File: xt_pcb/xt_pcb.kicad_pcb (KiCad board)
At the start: 2 copper layers, 197 parts, among them J1 Conn_01x04_Socket, SW1 SW_Push, SW10 SW_Push, SW11 SW_Push, SW12 SW_Push, SW13 SW_Push, SW14 SW_Push, SW15 SW_Push, SW16 SW_Push, SW17 SW_Push, SW19 SW_Push, SW2 SW_Push, SW20 SW_Push, SW21 SW_Push, SW22 SW_Push, SW23 SW_Push, SW24 SW_Push, SW25 SW_Push, SW26 SW_Push, SW27 SW_Push, SW28 SW_Push, SW29 SW_Push, SW3 SW_Push, SW30 SW_Push, SW31 SW_Push, SW32 SW_Push, SW33 SW_Push, SW34 SW_Push, SW35 SW_Push, SW36 SW_Push, SW37 SW_Push, SW38 SW_Push, SW39 SW_Push, SW4 SW_Push, SW40 SW_Push, SW41 SW_Push, SW42 SW_Push, SW43 SW_Push, SW44 SW_Push, SW45 SW_Push, SW46 SW_Push, SW47 SW_Push, SW48 SW_Push, SW49 SW_Push, SW5 SW_Push, SW50 SW_Push, SW51 SW_Push, SW52 SW_Push, SW53 SW_Push, SW54 SW_Push, SW55 SW_Push, SW56 SW_Push, SW57 SW_Push, SW58 SW_Push, SW59 SW_Push, SW6 SW_Push, SW60 SW_Push, SW61 SW_Push, SW62 SW_Push, SW63 SW_Push, SW64 SW_Push, SW66 SW_Push, SW67 SW_Push, SW68 SW_Push, SW69 SW_Push, SW7 SW_Push, SW70 SW_Push, SW71 SW_Push, SW72 SW_Push, SW73 SW_Push, SW74 SW_Push, SW75 SW_Push, SW76 SW_Push, SW77 SW_Push, SW78 SW_Push, SW79 SW_Push, SW8 SW_Push, SW80 SW_Push, SW81 SW_Push, SW82 SW_Push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

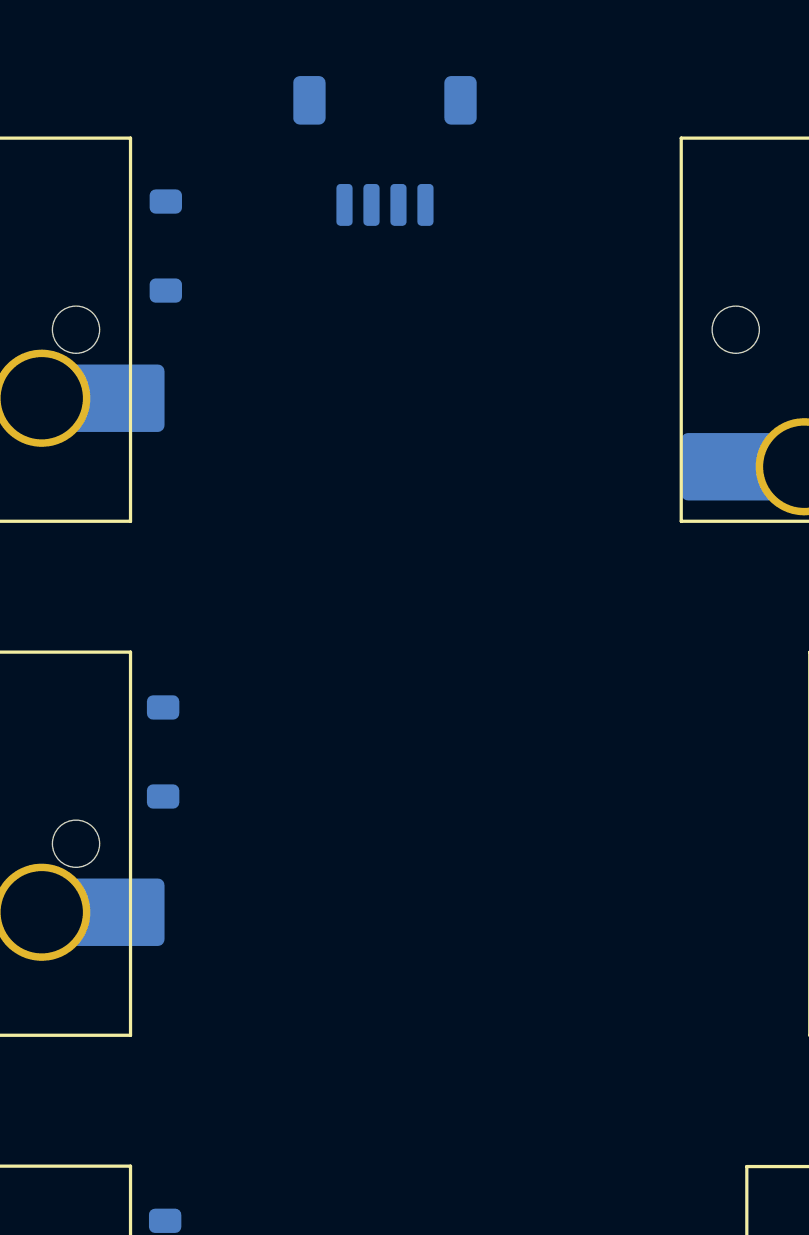
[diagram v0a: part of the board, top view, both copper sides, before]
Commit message: Type C Receptible + EDB added
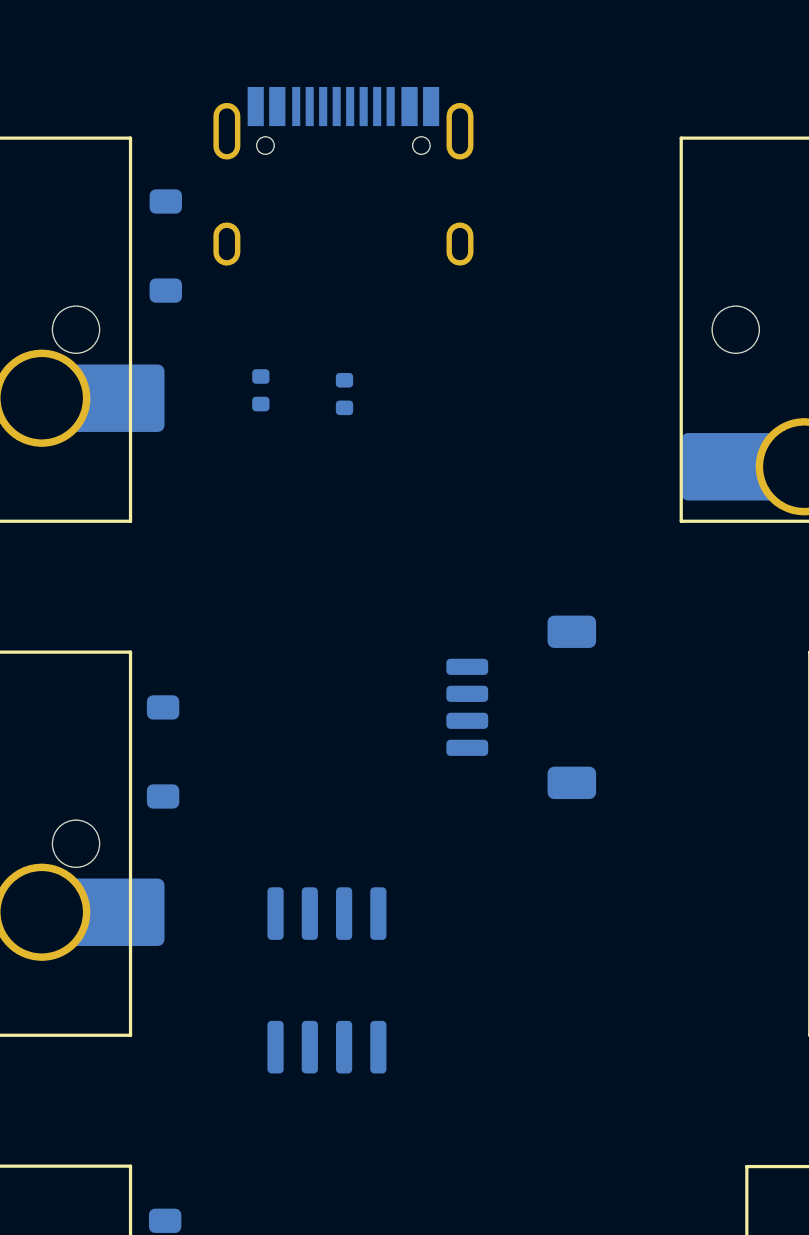
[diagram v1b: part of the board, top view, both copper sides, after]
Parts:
- added J2: USB_C_Receptacle_USB2.0_16P, Connector_USB:USB_C_Receptacle_HRO_TYPE-C-31-M-12, B.Cu at (84.6, 22.8)
- added R4: 5k1, Resistor_SMD:R_0402_1005Metric, B.Cu at (84.6, 29.5)
- added R5: 5k1, Resistor_SMD:R_0402_1005Metric, B.Cu at (81.5, 29.3)
- added U3: USB6B1, Package_SO:SOIC-8_3.9x4.9mm_P1.27mm, B.Cu at (84.0, 51.2)
- moved J1 21.2 mm to (91.2, 41.1), turned to -90 degrees

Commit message: basic tracing added to pcb
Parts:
- BT1, C1, C2, C3, C4, C5, C6, C7, C8, R1, R2, R3, U1, Y1: moved to B.Cu
- moved C4 225.7 mm to (94.9, 129.9), turned to 90 degrees
- moved C5 212.5 mm to (107.1, 140.4), turned to 90 degrees
- moved U1 165.8 mm to (100.2, 147.9), turned to 180 degrees
- moved R1 159.4 mm to (86.3, 121.1), turned to -90 degrees
- moved C8 144.2 mm to (152.2, 181.6), turned to 180 degrees
- moved Y1 126.1 mm to (197.4, 126.0), turned to 180 degrees
- moved R2 118.7 mm to (124.9, 136.3)
- moved C1 116.5 mm to (187.3, 117.8), turned to -90 degrees
- moved C2 115.4 mm to (189.2, 117.8), turned to -90 degrees
- moved R3 115.2 mm to (131.0, 130.9), turned to 180 degrees
- moved C3 114.4 mm to (191.2, 117.8), turned to -90 degrees
- moved C6 102.8 mm to (197.6, 136.0), turned to -90 degrees
- moved C7 101.3 mm to (199.7, 136.0), turned to 90 degrees
- moved BT1 89.3 mm to (210.9, 117.8)
- moved U2 50.5 mm to (264.4, 105.9), turned to 90 degrees
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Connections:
- J2 pad A1: Net-(J2-GND-PadA1) -> GND
- J2 pad A12: Net-(J2-GND-PadA1) -> GND
- J2 pad B1: Net-(J2-GND-PadA1) -> GND
- J2 pad B12: Net-(J2-GND-PadA1) -> GND
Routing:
- net R5: track 0.00 -> 418.7 mm
- net R3: track 0.00 -> 411.1 mm
- net R2: track 0.00 -> 399.6 mm
- net R1: track 0.00 -> 396.5 mm, vias 0 -> 2
- net R4: track 0.00 -> 393.9 mm
- net C8: track 0.00 -> 110.8 mm, vias 0 -> 1
- net C13: track 0.00 -> 105.7 mm
- net C12: track 0.00 -> 103.7 mm
- net C4: track 0.00 -> 95.4 mm
- net C15: track 0.00 -> 94.4 mm
- net C5: track 0.00 -> 94.3 mm
- net C16: track 0.00 -> 92.6 mm
- net GND: track 0.00 -> 83.0 mm, vias 0 -> 8
- net D-: track 0.00 -> 82.1 mm, vias 0 -> 3
- net VBUS: track 0.00 -> 81.3 mm, vias 0 -> 4
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
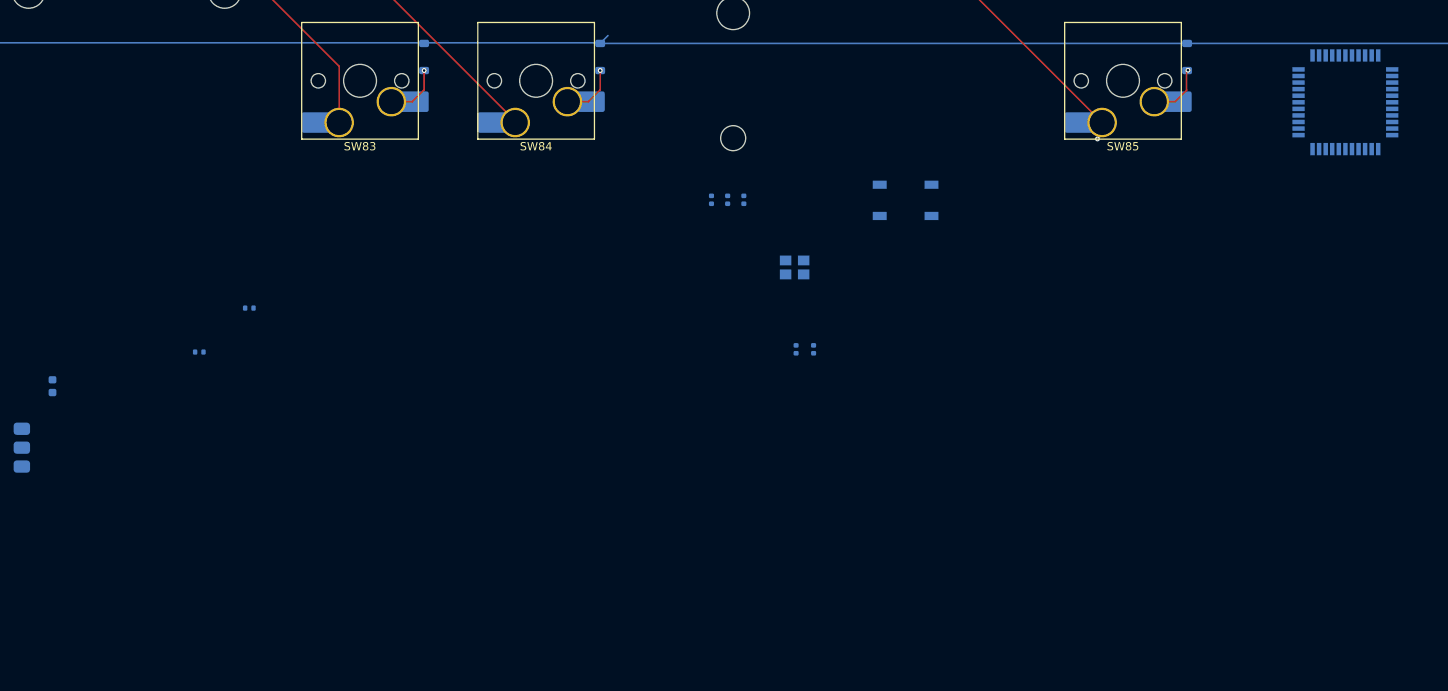
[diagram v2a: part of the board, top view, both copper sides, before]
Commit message: Switch matrix labels
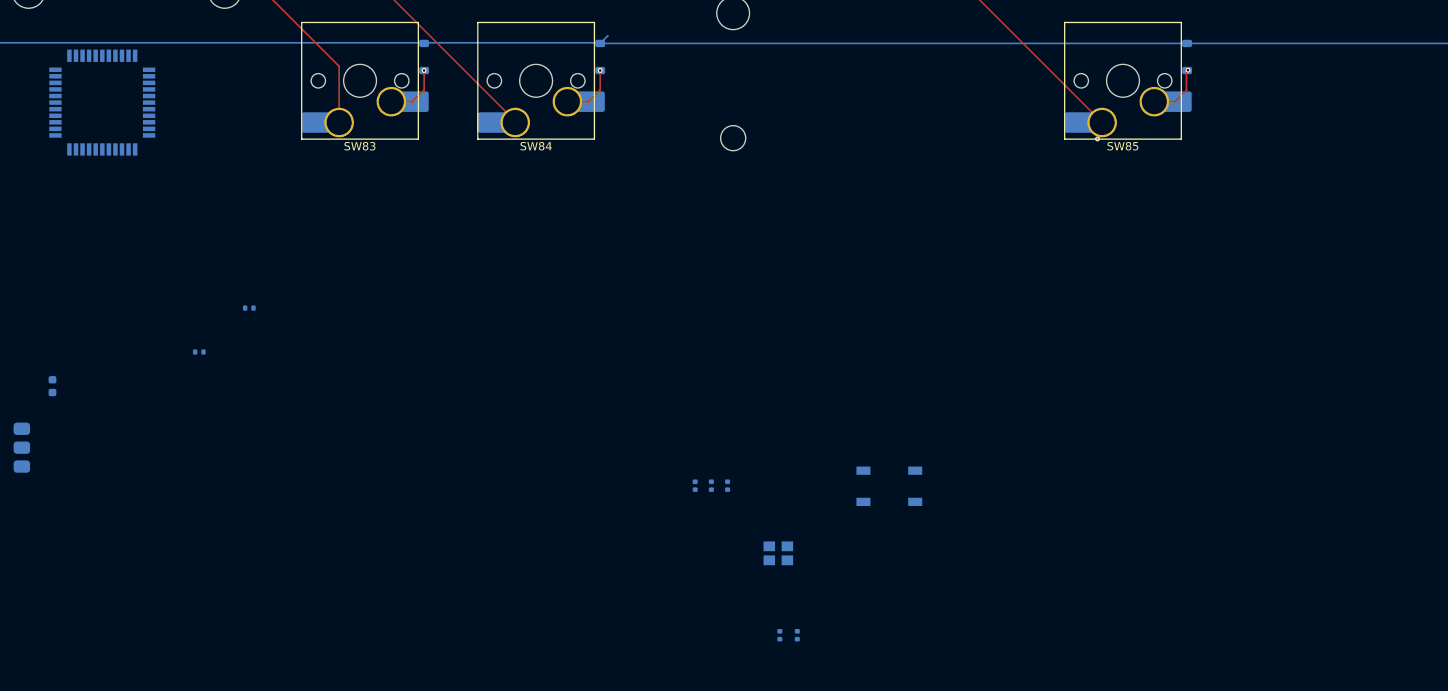
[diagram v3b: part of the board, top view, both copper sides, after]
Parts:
- moved U2 151.3 mm to (113.1, 105.9)
- moved C2 34.9 mm to (187.3, 152.6)
- moved C3 34.9 mm to (189.2, 152.6)
- moved BT1 34.9 mm to (208.9, 152.6)
- moved C1 34.9 mm to (185.3, 152.6)
- moved Y1 34.9 mm to (195.4, 160.8)
- moved C6 34.9 mm to (195.6, 170.8)
- moved C7 34.9 mm to (197.7, 170.8)

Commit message: tracing finished
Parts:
- moved R1 187.3 mm to (272.6, 101.0)
- moved U2 146.8 mm to (259.9, 103.2)
- moved U1 120.8 mm to (212.8, 104.3), turned to 0 degrees
- moved C8 119.7 mm to (248.4, 110.3), turned to 90 degrees
- moved C4 110.9 mm to (202.1, 101.9), turned to 180 degrees
- moved R2 105.4 mm to (227.0, 110.0)
- moved C5 101.4 mm to (202.2, 105.5), turned to 180 degrees
- moved R3 97.9 mm to (227.0, 111.5), turned to 0 degrees
- moved C1 96.4 mm to (272.4, 111.2), turned to 0 degrees
- moved C2 95.5 mm to (272.4, 109.2), turned to 0 degrees
- moved C3 94.7 mm to (272.4, 107.3), turned to 0 degrees
- moved BT1 85.8 mm to (279.7, 104.2), turned to -90 degrees
- moved C6 68.3 mm to (222.2, 107.8), turned to 90 degrees
- moved C7 66.8 mm to (220.1, 107.8), turned to -90 degrees
- moved Y1 63.2 mm to (221.1, 103.1), turned to 90 degrees
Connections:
- U2 pad 1: unconnected-(U2-PE6-Pad1) -> C15
- U2 pad 10: unconnected-(U2-PB2-Pad10) -> C4
- U2 pad 11: unconnected-(U2-PB3-Pad11) -> C1
- U2 pad 12: unconnected-(U2-PB7-Pad12) -> C8
- U2 pad 18: unconnected-(U2-PD0-Pad18) -> C3
- U2 pad 19: unconnected-(U2-PD1-Pad19) -> C6
- U2 pad 20: unconnected-(U2-PD2-Pad20) -> C7
- U2 pad 21: unconnected-(U2-PD3-Pad21) -> R4
- U2 pad 22: unconnected-(U2-PD5-Pad22) -> R5
- U2 pad 25: unconnected-(U2-PD4-Pad25) -> R2
- U2 pad 26: unconnected-(U2-PD6-Pad26) -> R3
- U2 pad 27: unconnected-(U2-PD7-Pad27) -> R1
- U2 pad 28: unconnected-(U2-PB4-Pad28) -> C9
- U2 pad 29: unconnected-(U2-PB5-Pad29) -> C10
- U2 pad 30: unconnected-(U2-PB6-Pad30) -> C11
- U2 pad 31: unconnected-(U2-PC6-Pad31) -> C12
- U2 pad 32: unconnected-(U2-PC7-Pad32) -> C13
- U2 pad 33: unconnected-(U2-~{HWB}/PE2-Pad33) -> C14
- U2 pad 38: unconnected-(U2-PF5-Pad38) -> C19
- U2 pad 39: unconnected-(U2-PF4-Pad39) -> C18
- U2 pad 40: unconnected-(U2-PF1-Pad40) -> C17
- U2 pad 41: unconnected-(U2-PF0-Pad41) -> C16
- U2 pad 8: unconnected-(U2-PB0-Pad8) -> C5
- U2 pad 9: unconnected-(U2-PB1-Pad9) -> C2
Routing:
- net VBUS: track 81.3 -> 343.9 mm, vias 4 -> 15
- net GND: track 83.0 -> 337.7 mm, vias 8 -> 25
- net C1: track 76.2 -> 317.1 mm, vias 0 -> 6
- net C2: track 76.2 -> 297.4 mm, vias 0 -> 7
- net C19: track 76.2 -> 288.5 mm, vias 0 -> 2
- net C18: track 76.2 -> 252.1 mm, vias 0 -> 4
- net C17: track 76.2 -> 241.4 mm, vias 0 -> 4
- net D-: track 82.1 -> 242.4 mm, vias 3 -> 4
- net C3: track 76.6 -> 235.5 mm, vias 0 -> 3
- net D+: track 59.8 -> 212.3 mm, vias 7 -> 10
- net C4: track 95.4 -> 231.6 mm, vias 0 -> 7
- net +5V: track 56.1 -> 186.8 mm, vias 1 -> 6
- net C16: track 92.6 -> 216.0 mm, vias 0 -> 4
- net C5: track 94.3 -> 208.0 mm, vias 0 -> 9
- net C15: track 94.4 -> 202.0 mm, vias 0 -> 4
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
